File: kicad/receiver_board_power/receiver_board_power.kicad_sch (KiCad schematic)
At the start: 8 parts, among them J1 Battery Conn, Q1 FQP27P06, SW1 On/Off, U1 2S BMS, U2 5V Buck

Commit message: Update GPIO assignments and complete first-pass PCB layout
Swap motor control IN1/IN2 pins to simplify PCB routing:
- Motor 1: IN1 GPIO4, IN2 GPIO3 (was IN1 GPIO3, IN2 GPIO4)
- Motor 2: IN1 GPIO7, IN2 GPIO6 (was IN1 GPIO6, IN2 GPIO7)

Updated documentation:
- lib/hardware.py: Motor GPIO pin definitions
- README.md: Receiver GPIO assignment table
- receiver/README.md: Hardware pin descriptions

PCB design progress:
- Controller board: First-pass layout and routing complete
- Receiver logic board: First-pass layout and routing complete
- Receiver power board: First-pass layout and routing complete
- All decoupling capacitors added (470µF on TB6612 VM, 0.1µF on logic)
- Verified netlists: power, ground, GPIO, and board-to-board connections

Design notes:
- Potentiometer uses pin socket for off-board panel mount (bent legs)
- P-FET uses bent legs for mechanical positioning in enclosure
- P-FET on logic board near high-current loads (smart placement)
- Board-to-board connector properly routes all 6 signals

Co-Authored-By: Claude Sonnet 4.5 <noreply@anthropic.com>
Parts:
- removed Q1: FQP27P06, Package_TO_SOT_THT:TO-220-3_Vertical, symbol Transistor_FET:FQP27P06
- removed R1: 10k, Resistor_THT:R_Axial_DIN0207_L6.3mm_D2.5mm_P7.62mm_Horizontal, symbol Device:R
- added J2: B2B, Connector_PinHeader_2.54mm:PinHeader_1x06_P2.54mm_Vertical, symbol Connector:Conn_01x06_Pin
- J1: footprint Connector_PinHeader_2.54mm:PinHeader_1x02_P2.54mm_Horizontal -> Connector_PinHeader_2.54mm:PinHeader_1x02_P2.54mm_Vertical
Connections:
- net 7v4_BMS: now also J2.2 (Pin_2)
- net GND: now also J2.3 (Pin_3)
- net LED_ESP: now also J2.6 (Pin_6)
- net PWR_SW: now also J2.4 (Pin_4)
- net 5V_BUCK renamed 5v_BUCK
- net 5v_BUCK: now also J2.5 (Pin_5)
- net 7V4_FET renamed 7v4_FET
- net 7v4_FET: now also J2.1 (Pin_1)
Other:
- moved on the sheet: SW1

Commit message: Add battery monitor connector and update receiver power board layout
- Add 3-pin battery monitor connector (J3) to receiver power board
  - Connected to BMS balance leads (B+, BM, B-)
  - Enables individual cell voltage monitoring
- Update receiver power board PCB layout and routing
- Export updated netlists for all three boards
- Add BMS reference image (bom/images/2S_BMS.jpg)
- Add *.lck to .gitignore to exclude KiCad lock files

Co-Authored-By: Claude Sonnet 4.5 <noreply@anthropic.com>
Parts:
- added J3: Battery Mon, Connector_PinHeader_2.54mm:PinHeader_1x03_P2.54mm_Vertical, symbol Connector:Conn_01x03_Pin
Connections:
- net at U1.7 (B+): now also J3.1 (Pin_1)
- net at U1.8 (BM): now also J3.2 (Pin_2)
- net at U1.9 (B-): now also J3.3 (Pin_3)
- no-connect marks 7 -> 4
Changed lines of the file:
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@@
 	(paper "A4")
 	(no_connect
-		(at 101.6 81.28)
-	)
-	(no_connect
 		(at 180.34 88.9)
-	)
-	(no_connect
-		(at 100.33 81.28)
 	)
 	(no_connect
@@
 	)
 	(no_connect
-		(at 102.87 81.28)
-	)
-	(no_connect
 		(at 93.98 73.66)
 	)
@@
 	(wire
 		(pts
+			(xy 99.06 87.63) (xy 100.33 87.63)
+		)
+		(stroke
+			(width 0)
+			(type default)
+		)
+	)
+	(wire
+		(pts
 			(xy 105.41 85.09) (xy 105.41 81.28)
 		)
@@
 	(wire
 		(pts
+			(xy 104.14 87.63) (xy 102.87 87.63)
+		)
+		(stroke
+			(width 0)
+			(type default)
+		)
+	)
+	(wire
+		(pts
 			(xy 153.67 97.79) (xy 148.59 97.79)
 		)
@@
 	(wire
 		(pts
+			(xy 102.87 87.63) (xy 102.87 81.28)
+		)
+		(stroke
+			(width 0)
+			(type default)
+		)
+	)
+	(wire
+		(pts
 			(xy 100.33 64.77) (xy 97.79 64.77)
 		)
@@
 	(wire
 		(pts
+			(xy 101.6 81.28) (xy 101.6 87.63)
+		)
+		(stroke
+			(width 0)
+			(type default)
+		)
+	)
+	(wire
+		(pts
 			(xy 185.42 66.04) (xy 189.23 66.04)
 		)
@@
 		(pts
 			(xy 185.42 68.58) (xy 189.23 68.58)
+		)
+		(stroke
+			(width 0)
+			(type default)
+		)
+	)
+	(wire
+		(pts
+			(xy 100.33 87.63) (xy 100.33 81.28)
 		)
 		(stroke
@@
 					(unit 1)
 				)
+			)
+		)
+	)
+	(symbol
+		(lib_id "Connector:Conn_01x03_Pin")
+		(at 101.6 92.71 90)
+		(unit 1)
+		(exclude_from_sim no)
+		(in_bom yes)
+		(on_board yes)
+		(dnp no)
+		(fields_autoplaced yes)
+		(property "Reference" "J3"
+			(at 101.6 95.25 90)
+			(effects
+				(font
+					(size 1.27 1.27)
+				)
+			)
+		)
+		(property "Value" "Battery Mon"
+			(at 101.6 97.79 90)
+			(effects
+				(font
+					(size 1.27 1.27)
+				)
+			)
+		)
+		(property "Footprint" "Connector_PinHeader_2.54mm:PinHeader_1x03_P2.54mm_Vertical"
+			(at 101.6 92.71 0)
+			(effects
+				(font
+					(size 1.27 1.27)
+				)
+				(hide yes)
+			)
+		)
+		(property "Datasheet" "~"
+			(at 101.6 92.71 0)
+			(effects
+				(font
+					(size 1.27 1.27)
+				)
+				(hide yes)
+			)
+		)
+		(property "Description" "Generic connector, single row, 01x03, script generated"
+			(at 101.6 92.71 0)
+			(effects
+				(font
+					(size 1.27 1.27)
+				)
+				(hide yes)
+			)
+		)
+		(pin "1"
+		)
+		(pin "3"
+		)
+		(pin "2"
+		)
+		(instances
+			(project ""
+				(path "/c65229a9-37b7-4cd8-a90e-78faaca9b050"
+					(reference "J3")
+					(unit 1)
+				)

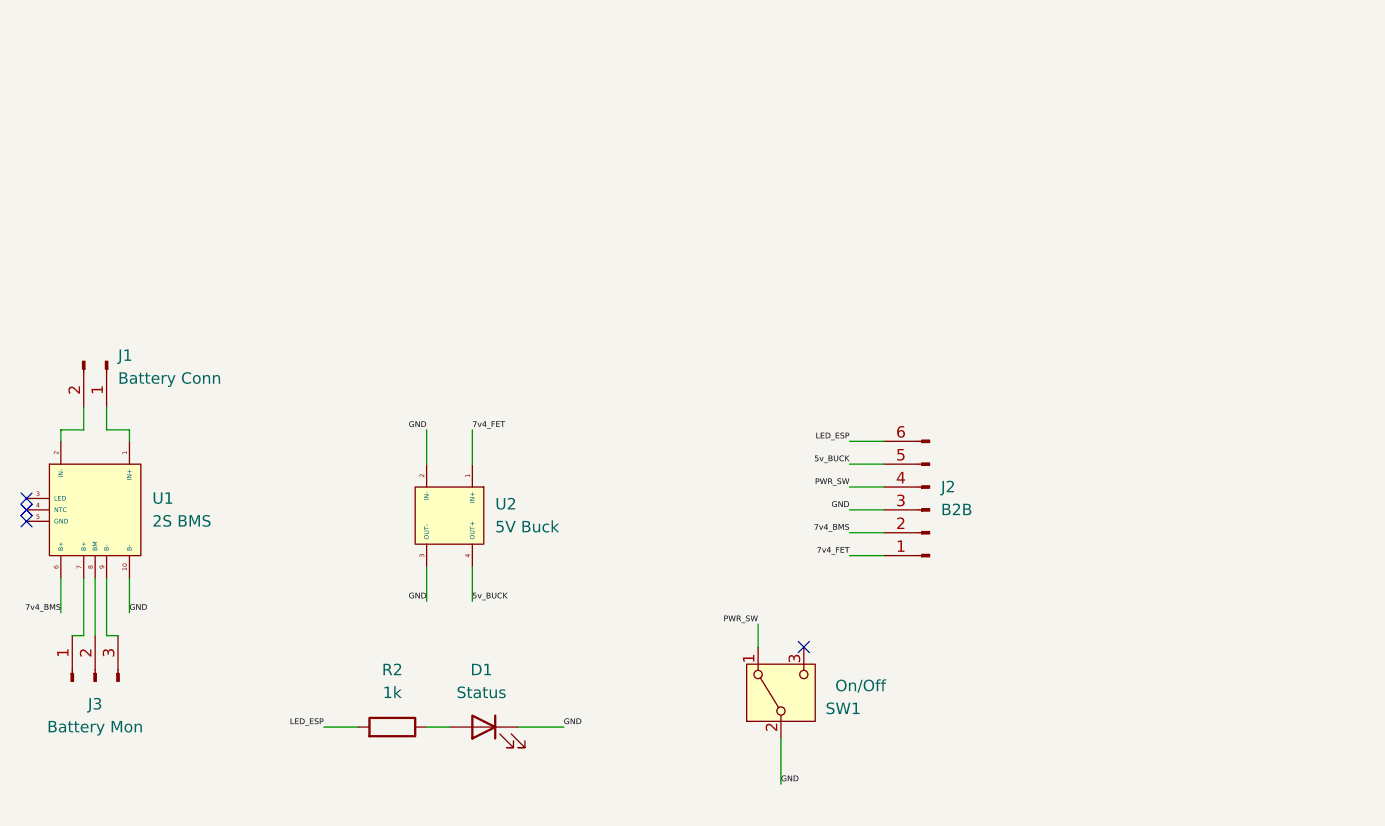
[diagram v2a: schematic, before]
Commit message: Remove BMS and reorganize receiver boards for external charging
Major schematic and layout revision based on EE review:

- Remove BMS from receiver design; pivot to external LiPo charging
- Reorganize components between power and logic boards:
  - Logic board: P-FET power switch, buck converter, UI (LED/button), debug UART
  - Power board: ESP32-C3, motor driver, battery monitoring
- Add voltage dividers for 2S LiPo monitoring (B+ and BM)
  - Safe ADC voltages: B+ = 2.36V max, BM = 2.47V max
- Add debug UART headers (GPIO20/21) for serial output when USB unavailable
- Fix P-FET drain connection to properly power both buck and motor system
- Update B2B connectors to dual 6-pin configuration (signal + power)
- Minor controller board PCB layout adjustments

Co-Authored-By: Claude Sonnet 4.5 <noreply@anthropic.com>
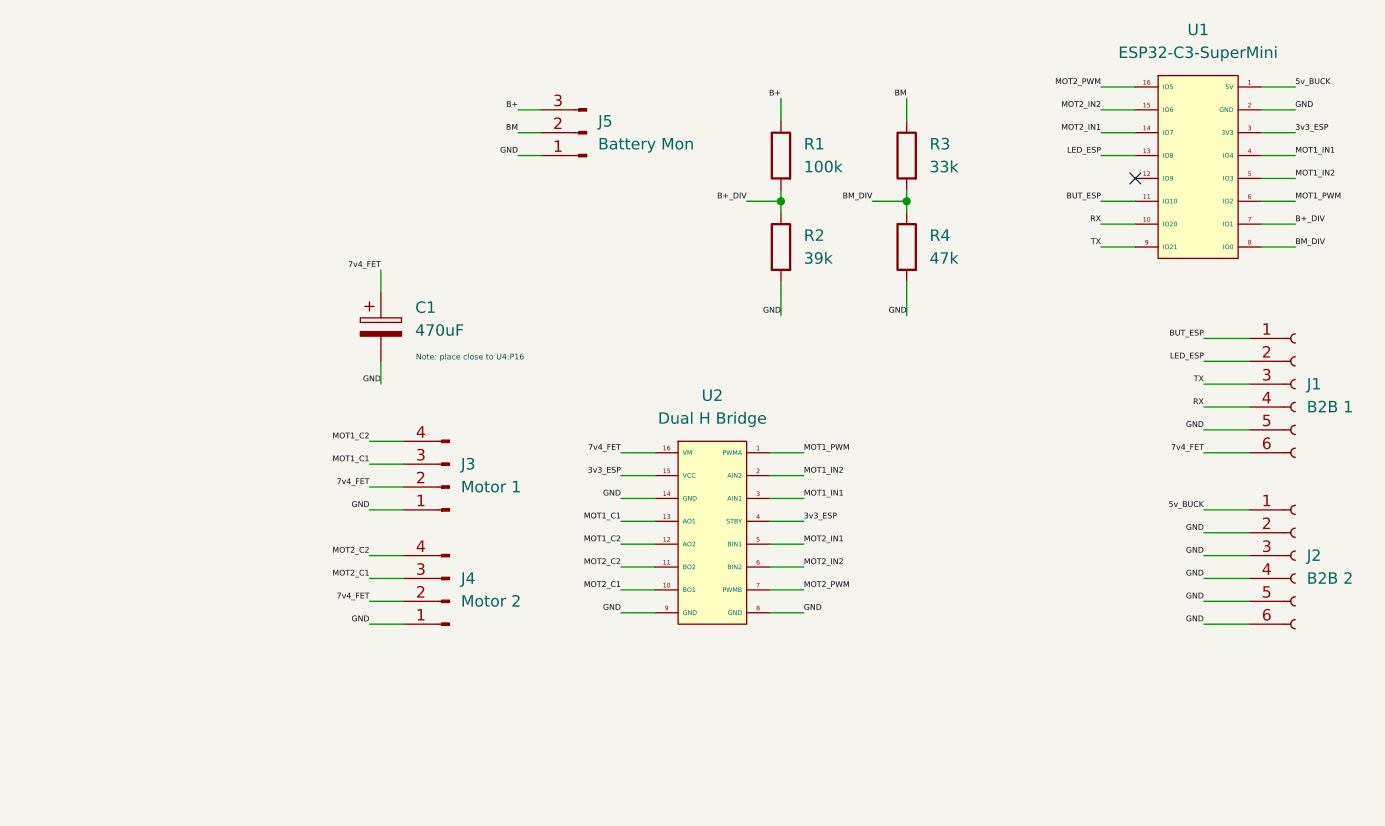
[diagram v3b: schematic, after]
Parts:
- removed D1: Status, LED_THT:LED_D5.0mm, symbol Device:LED
- removed J1: Battery Conn, Connector_PinHeader_2.54mm:PinHeader_1x02_P2.54mm_Vertical, symbol Connector:Conn_01x02_Pin
- removed J2: B2B, Connector_PinHeader_2.54mm:PinHeader_1x06_P2.54mm_Vertical, symbol Connector:Conn_01x06_Pin
- removed J3: Battery Mon, Connector_PinHeader_2.54mm:PinHeader_1x03_P2.54mm_Vertical, symbol Connector:Conn_01x03_Pin
- removed SW1: On/Off, ESP32_Lego_PF:Slide_Switch_SPDT_12D00G, symbol Switch:SW_SPDT
- removed U1: 2S BMS, ESP32_Lego_PF:2S BMS, symbol ESP32_Lego_PF:2S_BMS
- removed U2: 5V Buck, ESP32_Lego_PF:MP1584EN, symbol ESP32_Lego_PF:MP1584EN
- added C1: 470uF, Capacitor_THT:CP_Radial_D8.0mm_P5.00mm, symbol Device:C_Polarized
- added J1: B2B 1, Connector_PinSocket_2.54mm:PinSocket_1x06_P2.54mm_Vertical, symbol Connector:Conn_01x06_Socket
- added J2: B2B 2, Connector_PinSocket_2.54mm:PinSocket_1x06_P2.54mm_Vertical, symbol Connector:Conn_01x06_Socket
- added J3: Motor 1, Connector_JST:JST_XH_B4B-XH-A_1x04_P2.50mm_Vertical, symbol Connector:Conn_01x04_Pin
- added J4: Motor 2, Connector_JST:JST_XH_B4B-XH-A_1x04_P2.50mm_Vertical, symbol Connector:Conn_01x04_Pin
- added J5: Battery Mon, Connector_PinHeader_2.54mm:PinHeader_1x03_P2.54mm_Vertical, symbol Connector:Conn_01x03_Pin
- added R1: 100k, Resistor_THT:R_Axial_DIN0207_L6.3mm_D2.5mm_P7.62mm_Horizontal, symbol Device:R
- added R3: 33k, Resistor_THT:R_Axial_DIN0207_L6.3mm_D2.5mm_P7.62mm_Horizontal, symbol Device:R
- added R4: 47k, Resistor_THT:R_Axial_DIN0207_L6.3mm_D2.5mm_P7.62mm_Horizontal, symbol Device:R
- added U1: ESP32-C3-SuperMini, ESP32_Lego_PF:ESP32-C3-SuperMini, symbol ESP32_Lego_PF:ESP32-C3-SuperMini
- added U2: Dual H Bridge, ESP32_Lego_PF:TB6612FNG, symbol ESP32_Lego_PF:TB6612FNG
- R2: value 1k -> 39k
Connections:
- net 5v_BUCK: now also J2.1 (Pin_1), U1.1 (5V)
- net 7v4_FET: now also C1.1, J1.6 (Pin_6), J3.2 (Pin_2), J4.2 (Pin_2), U2.16 (VM)
- net GND: now also R2.2, C1.2, J1.5 (Pin_5), J2.2 (Pin_2), J2.3 (Pin_3), J2.4 (Pin_4), J2.5 (Pin_5), J2.6 (Pin_6), J3.1 (Pin_1), J4.1 (Pin_1), J5.1 (Pin_1), R4.2, U1.2 (GND), U2.14 (GND), U2.8 (GND), U2.9 (GND)
- net LED_ESP: now also J1.2 (Pin_2), U1.13 (IO8); no longer R2.2
- net B+_DIV: now reaches R2.1
- net B+_DIV: now also R1.2, U1.7 (IO1)
- new net 3v3_ESP: U1.3 (3V3), U2.15 (VCC), U2.4 (STBY)
- new net B+: J5.3 (Pin_3), R1.1
- new net BM: J5.2 (Pin_2), R3.1
- new net BM_DIV: R3.2, R4.1, U1.8 (IO0)
- new net BUT_ESP: J1.1 (Pin_1), U1.11 (IO10)
- new net MOT1_C1: J3.3 (Pin_3), U2.13 (AO1)
- new net MOT1_C2: J3.4 (Pin_4), U2.12 (AO2)
- new net MOT1_IN1: U1.4 (IO4), U2.3 (AIN1)
- new net MOT1_IN2: U1.5 (IO3), U2.2 (AIN2)
- new net MOT1_PWM: U1.6 (IO2), U2.1 (PWMA)
- new net MOT2_C1: J4.3 (Pin_3), U2.10 (BO1)
- new net MOT2_C2: J4.4 (Pin_4), U2.11 (BO2)
- new net MOT2_IN1: U1.14 (IO7), U2.5 (BIN1)
- new net MOT2_IN2: U1.15 (IO6), U2.6 (BIN2)
- new net MOT2_PWM: U1.16 (IO5), U2.7 (PWMB)
- new net RX: J1.4 (Pin_4), U1.10 (IO20)
- new net TX: J1.3 (Pin_3), U1.9 (IO21)
- no-connect marks 4 -> 1
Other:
- note added: "Note: place close to U4:P16"

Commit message: Add battery monitoring module with unit tests and swap B+/BM GPIOs
Add lib/battery.py for 2S LiPo voltage monitoring via hardware voltage
dividers (B+ on GPIO0, BM on GPIO1). Includes per-cell voltage tracking,
status detection (OK/LOW/CRITICAL/IMBALANCED), and percentage estimation.

Add tests/test_battery.py with 25 unit tests covering voltage conversion,
status thresholds, percentage clamping, cell imbalance, and edge cases.

Update deploy scripts, documentation, and KiCad schematic/PCB to swap
B+ and BM GPIO assignments for cleaner PCB routing.

Co-Authored-By: Claude Opus 4.5 <noreply@anthropic.com>
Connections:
- net B+_DIV: now also U1.8 (IO0); no longer U1.7 (IO1)
- net BM_DIV: now also U1.7 (IO1); no longer U1.8 (IO0)
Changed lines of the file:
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@@
 		)
 	)
-	(label "B+_DIV"
+	(label "BM_DIV"
 		(at 234.95 41.91 0)
 		(effects
@@
 		)
 	)
-	(label "BM_DIV"
+	(label "B+_DIV"
 		(at 234.95 44.45 0)
 		(effects
